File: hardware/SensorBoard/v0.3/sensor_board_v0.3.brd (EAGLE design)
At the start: 46.8 x 39.9 mm, 58 parts, among them IC1 MCP1703CB, IC2 MCP1703CB, J3 USB-MICROB, Q1 MMBT5088-NPN, U1 ATMEGA328P, U2 TSL2561FN, U4 MPL115A, U5 FT231XS, Y1 16MHZ

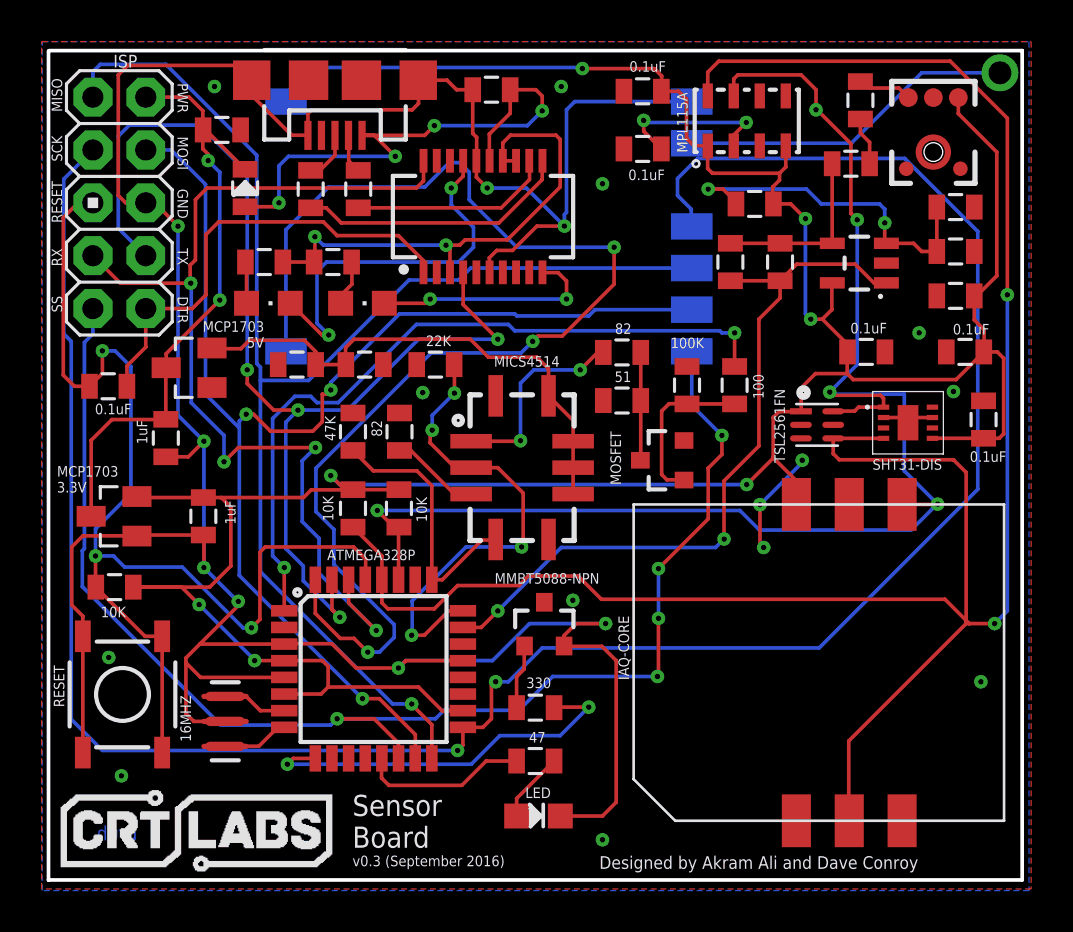
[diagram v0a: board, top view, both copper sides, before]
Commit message: Moved hidden labels to tNames layer
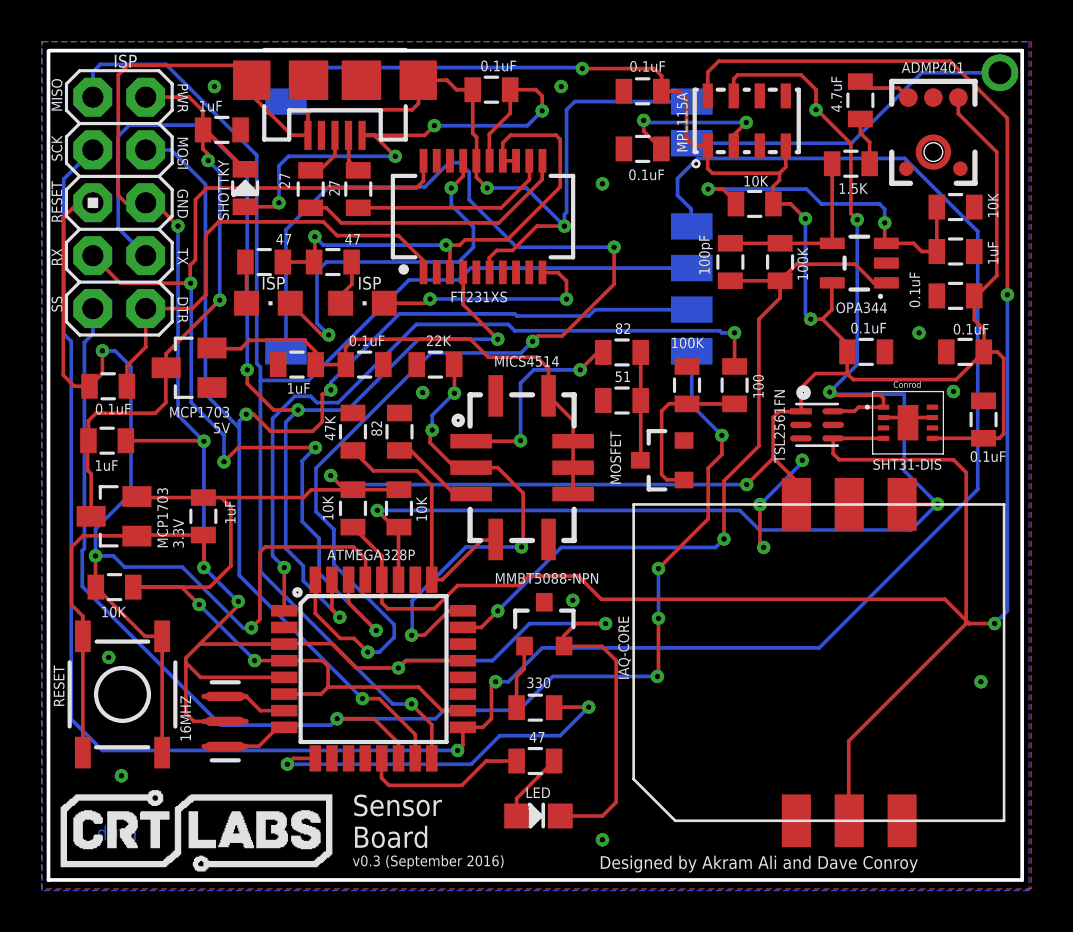
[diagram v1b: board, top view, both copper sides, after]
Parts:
- moved C1 2.82 mm to (8.71, 27.7), turned to 0 degrees
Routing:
- net GND: track 150.7 -> 152.3 mm
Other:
- board text added: "Conrod"

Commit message: Moved labels to _tsilk layer (121)
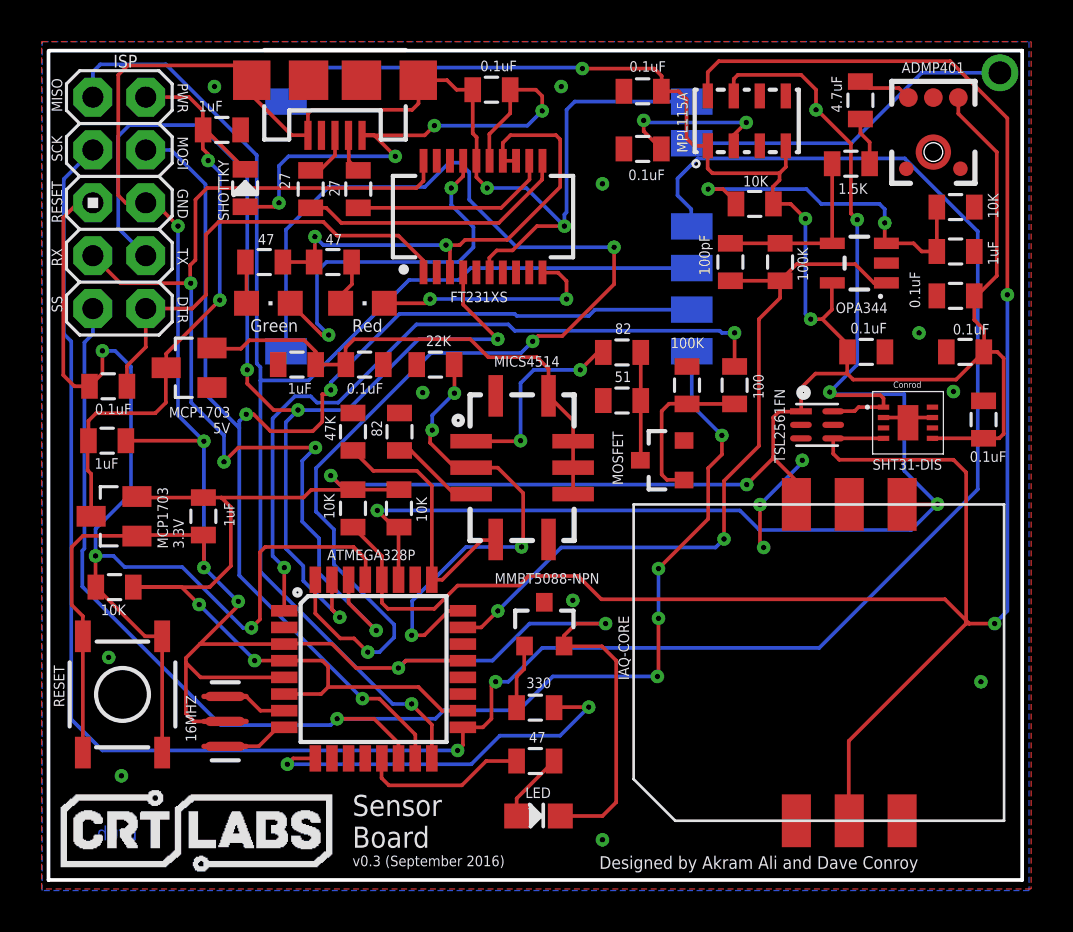
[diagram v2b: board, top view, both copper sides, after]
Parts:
- renumbered LED1 to RX, LED3 to TX
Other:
- board text added: "Green"
- board text added: "Red"

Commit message: Adjusted some traces
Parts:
- moved R8 4.12 mm to (41.2, 32.2), turned to 270 degrees
- moved C2 2.56 mm to (41.2, 36.0)
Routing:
- net N$10: track 8.73 -> 13.8 mm
- net D2: track 61.3 -> 58.6 mm
- net A0: track 36.1 -> 35.1 mm
